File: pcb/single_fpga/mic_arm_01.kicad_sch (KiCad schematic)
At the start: 18 parts, among them U10 IM72D128V01XTMA1, U11 IM72D128V01XTMA1, U12 IM72D128V01XTMA1, U13 IM72D128V01XTMA1, U14 IM72D128V01XTMA1, U15 IM72D128V01XTMA1, U16 IM72D128V01XTMA1, U17 IM72D128V01XTMA1, U18 CDCLVC1108PW

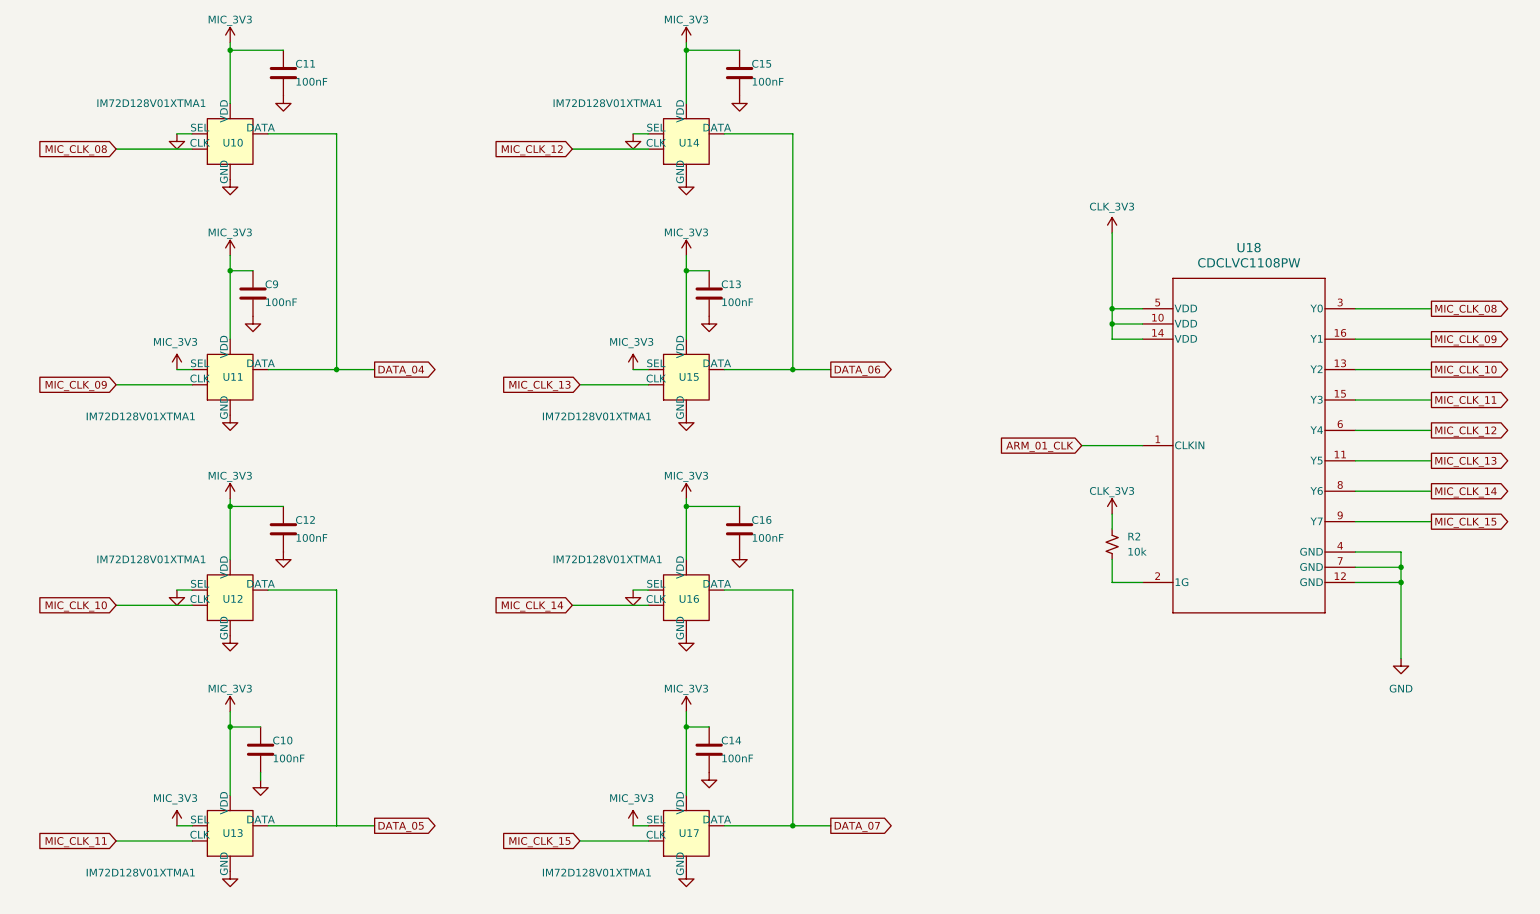
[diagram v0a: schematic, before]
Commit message: Changed mic symbol to improve readability.
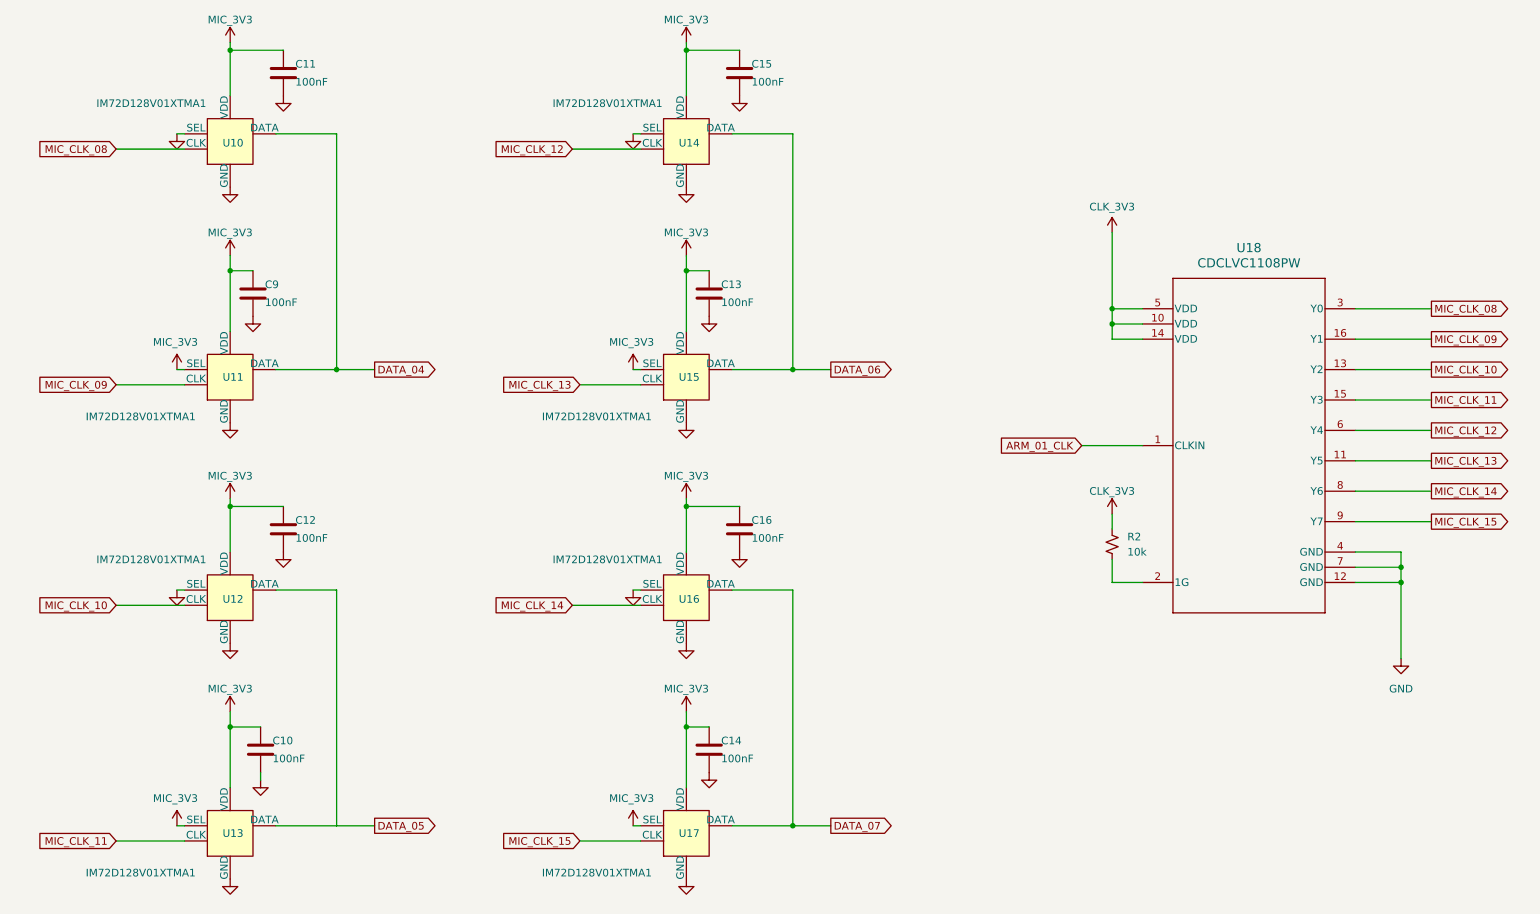
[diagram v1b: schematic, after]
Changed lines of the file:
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@@
 	(wire
 		(pts
-			(xy 127 119.38) (xy 129.54 119.38)
+			(xy 127 119.38) (xy 128.27 119.38)
 		)
 		(stroke
@@
 	(wire
 		(pts
-			(xy 118.11 161.29) (xy 129.54 161.29)
+			(xy 118.11 161.29) (xy 128.27 161.29)
 		)
 		(stroke
@@
 	(wire
 		(pts
-			(xy 59.69 66.04) (xy 59.69 77.47)
+			(xy 59.69 66.04) (xy 59.69 76.2)
 		)
 		(stroke
@@
 	(wire
 		(pts
-			(xy 135.89 105.41) (xy 135.89 114.3)
+			(xy 135.89 105.41) (xy 135.89 113.03)
 		)
 		(stroke
@@
 	(wire
 		(pts
-			(xy 116.84 45.72) (xy 129.54 45.72)
+			(xy 116.84 45.72) (xy 128.27 45.72)
 		)
 		(stroke
@@
 	(wire
 		(pts
-			(xy 40.64 121.92) (xy 53.34 121.92)
+			(xy 40.64 121.92) (xy 52.07 121.92)
 		)
 		(stroke
@@
 	(wire
 		(pts
-			(xy 66.04 158.75) (xy 77.47 158.75)
+			(xy 67.31 158.75) (xy 77.47 158.75)
 		)
 		(stroke
@@
 	(wire
 		(pts
-			(xy 59.69 142.24) (xy 59.69 153.67)
+			(xy 59.69 142.24) (xy 59.69 152.4)
 		)
 		(stroke
@@
 	(wire
 		(pts
-			(xy 153.67 43.18) (xy 142.24 43.18)
+			(xy 153.67 43.18) (xy 143.51 43.18)
 		)
 		(stroke
@@
 	(wire
 		(pts
-			(xy 50.8 82.55) (xy 53.34 82.55)
+			(xy 50.8 82.55) (xy 52.07 82.55)
 		)
 		(stroke
@@
 	(wire
 		(pts
-			(xy 153.67 119.38) (xy 142.24 119.38)
+			(xy 153.67 119.38) (xy 143.51 119.38)
 		)
 		(stroke
@@
 	(wire
 		(pts
-			(xy 40.64 85.09) (xy 53.34 85.09)
+			(xy 40.64 85.09) (xy 52.07 85.09)
 		)
 		(stroke
@@
 	(wire
 		(pts
-			(xy 116.84 121.92) (xy 129.54 121.92)
+			(xy 116.84 121.92) (xy 128.27 121.92)
 		)
 		(stroke
@@
 	(wire
 		(pts
-			(xy 77.47 43.18) (xy 66.04 43.18)
+			(xy 77.47 43.18) (xy 67.31 43.18)
 		)
 		(stroke
@@
 	(wire
 		(pts
-			(xy 127 43.18) (xy 129.54 43.18)
+			(xy 127 43.18) (xy 128.27 43.18)
 		)
 		(stroke
@@
 	(wire
 		(pts
-			(xy 127 158.75) (xy 129.54 158.75)
+			(xy 127 158.75) (xy 128.27 158.75)
 		)
 		(stroke
@@
 	(wire
 		(pts
-			(xy 59.69 105.41) (xy 59.69 114.3)
+			(xy 59.69 105.41) (xy 59.69 113.03)
 		)
 		(stroke
@@
 	(wire
 		(pts
-			(xy 135.89 29.21) (xy 135.89 38.1)
+			(xy 135.89 29.21) (xy 135.89 36.83)
 		)
 		(stroke
@@
 	(wire
 		(pts
-			(xy 118.11 85.09) (xy 129.54 85.09)
+			(xy 118.11 85.09) (xy 128.27 85.09)
 		)
 		(stroke
@@
 	(wire
 		(pts
-			(xy 40.64 45.72) (xy 53.34 45.72)
+			(xy 40.64 45.72) (xy 52.07 45.72)
 		)
 		(stroke
@@
 	(wire
 		(pts
-			(xy 50.8 158.75) (xy 53.34 158.75)
+			(xy 50.8 158.75) (xy 52.07 158.75)
 		)
 		(stroke
@@
 	(wire
 		(pts
-			(xy 50.8 43.18) (xy 53.34 43.18)
+			(xy 50.8 43.18) (xy 52.07 43.18)
 		)
 		(stroke
@@
 	(wire
 		(pts
-			(xy 135.89 66.04) (xy 135.89 77.47)
+			(xy 135.89 66.04) (xy 135.89 76.2)
 		)
 		(stroke
@@
 	(wire
 		(pts
-			(xy 77.47 119.38) (xy 66.04 119.38)
+			(xy 77.47 119.38) (xy 67.31 119.38)
 		)
 		(stroke
@@
 	(wire
 		(pts
-			(xy 142.24 82.55) (xy 153.67 82.55)
+			(xy 143.51 82.55) (xy 153.67 82.55)
 		)
 		(stroke
@@
 	(wire
 		(pts
-			(xy 50.8 119.38) (xy 53.34 119.38)
+			(xy 50.8 119.38) (xy 52.07 119.38)
 		)
 		(stroke
@@
 	(wire
 		(pts
-			(xy 66.04 82.55) (xy 77.47 82.55)
+			(xy 67.31 82.55) (xy 77.47 82.55)
 		)
 		(stroke
@@
 	(wire
 		(pts
-			(xy 142.24 158.75) (xy 153.67 158.75)
+			(xy 143.51 158.75) (xy 153.67 158.75)
 		)
 		(stroke
@@
 	(wire
 		(pts
-			(xy 40.64 161.29) (xy 53.34 161.29)
+			(xy 40.64 161.29) (xy 52.07 161.29)
 		)
 		(stroke
@@
 	(wire
 		(pts
-			(xy 59.69 29.21) (xy 59.69 38.1)
+			(xy 59.69 29.21) (xy 59.69 36.83)
 		)
 		(stroke
@@
 	(wire
 		(pts
-			(xy 127 82.55) (xy 129.54 82.55)
+			(xy 127 82.55) (xy 128.27 82.55)
 		)
 		(stroke
@@
 	(wire
 		(pts
-			(xy 135.89 142.24) (xy 135.89 153.67)
+			(xy 135.89 142.24) (xy 135.89 152.4)
 		)
 		(stroke
@@
 	(symbol
 		(lib_id "power:GND")
-		(at 59.69 50.8 0)
+		(at 59.69 52.07 0)
 		(unit 1)
 		(body_style 1)
@@
 	(symbol
 		(lib_id "power:GND")
-		(at 135.89 50.8 0)
+		(at 135.89 52.07 0)
 		(unit 1)
 		(body_style 1)
@@
 	(symbol
 		(lib_id "power:GND")
-		(at 59.69 166.37 0)
+		(at 59.69 167.64 0)
 		(unit 1)
 		(body_style 1)
@@
 	(symbol
 		(lib_id "power:GND")
-		(at 135.89 127 0)
+		(at 135.89 128.27 0)
 		(unit 1)
 		(body_style 1)
@@
 	(symbol
 		(lib_id "power:GND")
-		(at 135.89 166.37 0)
+		(at 135.89 167.64 0)
 		(unit 1)
 		(body_style 1)
@@
 	(symbol
 		(lib_id "power:GND")
-		(at 59.69 127 0)
+		(at 59.69 128.27 0)
 		(unit 1)
 		(body_style 1)
@@
 	(symbol
 		(lib_id "power:GND")
-		(at 59.69 90.17 0)
+		(at 59.69 91.44 0)
 		(unit 1)
 		(body_style 1)
@@
 	(symbol
 		(lib_id "power:GND")
-		(at 135.89 90.17 0)
+		(at 135.89 91.44 0)
 		(unit 1)
 		(body_style 1)

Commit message: Used new mic symbol and cleaned up.
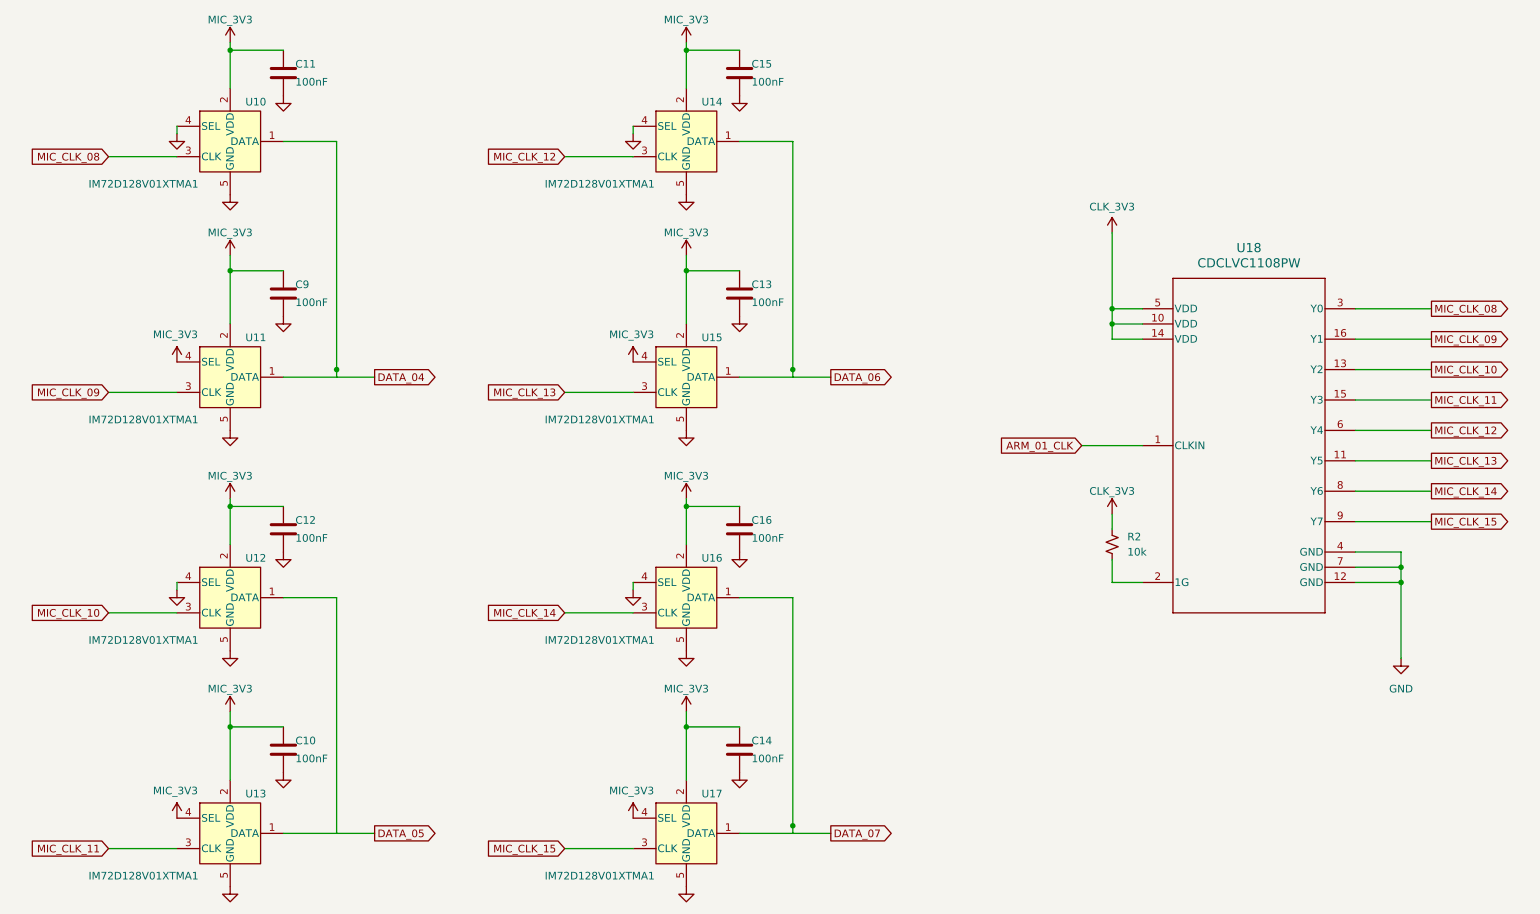
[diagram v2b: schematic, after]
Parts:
- U10, U11, U12, U13, U14, U15, U16, U17: footprint IM72D128:IFX-PG-LLGA-5-4 -> (none)
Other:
- moved on the sheet: C10, C13, C14, C9

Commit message: Fixed all DRC warnings.
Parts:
- U10, U11, U12, U13, U14, U15, U16, U17: footprint (none) -> IM72D128:IFX-PG-LLGA-5-4
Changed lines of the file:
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@@
 			)
 		)
-		(property "Footprint" ""
+		(property "Footprint" "IM72D128:IFX-PG-LLGA-5-4"
 			(at 59.69 44.45 0)
 			(hide yes)
@@
 			)
 		)
-		(property "Footprint" ""
+		(property "Footprint" "IM72D128:IFX-PG-LLGA-5-4"
 			(at 59.69 83.82 0)
 			(hide yes)
@@
 			)
 		)
-		(property "Footprint" ""
+		(property "Footprint" "IM72D128:IFX-PG-LLGA-5-4"
 			(at 135.89 83.82 0)
 			(hide yes)
@@
 			)
 		)
-		(property "Footprint" ""
+		(property "Footprint" "IM72D128:IFX-PG-LLGA-5-4"
 			(at 59.69 120.65 0)
 			(hide yes)
@@
 			)
 		)
-		(property "Footprint" ""
+		(property "Footprint" "IM72D128:IFX-PG-LLGA-5-4"
 			(at 135.89 44.45 0)
 			(hide yes)
@@
 			)
 		)
-		(property "Footprint" ""
+		(property "Footprint" "IM72D128:IFX-PG-LLGA-5-4"
 			(at 135.89 120.65 0)
 			(hide yes)
@@
 			)
 		)
-		(property "Footprint" ""
+		(property "Footprint" "IM72D128:IFX-PG-LLGA-5-4"
 			(at 59.69 160.02 0)
 			(hide yes)
@@
 			)
 		)
-		(property "Footprint" ""
+		(property "Footprint" "IM72D128:IFX-PG-LLGA-5-4"
 			(at 135.89 160.02 0)
 			(hide yes)

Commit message: Aligned mic and cap ref des numbers.
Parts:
- renumbered C9 to C10, C12 to C11, C10 to C12, C15 to C13, C13 to C14, C16 to C15, C14 to C16, C11 to C9, U11 to U10, U12 to U11, U13 to U12, U14 to U13, U15 to U14, U16 to U15, U17 to U16, U10 to U9, U18 to U98
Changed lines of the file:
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@@
 		(dnp no)
 		(fields_autoplaced yes)
-		(property "Reference" "U18"
+		(property "Reference" "U98"
 			(at 229.87 62.23 0)
 			(show_name no)
@@
 			(project "mic_array"
 				(path "/12638caa-1907-413e-8e98-06abbbf6ccbc/2e46394f-4741-4d6d-9c50-8b81cff9872d"
-					(reference "U18")
+					(reference "U98")
 					(unit 1)
 				)
@@
 		(in_pos_files yes)
 		(dnp no)
-		(property "Reference" "C13"
+		(property "Reference" "C14"
 			(at 146.78 68.35 0)
 			(show_name no)
@@
 			(project "mic_array"
 				(path "/12638caa-1907-413e-8e98-06abbbf6ccbc/2e46394f-4741-4d6d-9c50-8b81cff9872d"
-					(reference "C13")
+					(reference "C14")
 					(unit 1)
 				)
@@
 		(in_pos_files yes)
 		(dnp no)
-		(property "Reference" "C12"
+		(property "Reference" "C11"
 			(at 70.58 107.72 0)
 			(show_name no)
@@
 			(project "mic_array"
 				(path "/12638caa-1907-413e-8e98-06abbbf6ccbc/2e46394f-4741-4d6d-9c50-8b81cff9872d"
-					(reference "C12")
+					(reference "C11")
 					(unit 1)
 				)
@@
 		(in_pos_files yes)
 		(dnp no)
-		(property "Reference" "U10"
+		(property "Reference" "U9"
 			(at 62.23 37.846 0)
 			(show_name no)
@@
 			(project "mic_array"
 				(path "/12638caa-1907-413e-8e98-06abbbf6ccbc/2e46394f-4741-4d6d-9c50-8b81cff9872d"
-					(reference "U10")
+					(reference "U9")
 					(unit 1)
 				)
@@
 		(in_pos_files yes)
 		(dnp no)
-		(property "Reference" "U11"
+		(property "Reference" "U10"
 			(at 62.23 77.216 0)
 			(show_name no)
@@
 			(project "mic_array"
 				(path "/12638caa-1907-413e-8e98-06abbbf6ccbc/2e46394f-4741-4d6d-9c50-8b81cff9872d"
-					(reference "U11")
+					(reference "U10")
 					(unit 1)
 				)
@@
 		(in_pos_files yes)
 		(dnp no)
-		(property "Reference" "U15"
+		(property "Reference" "U14"
 			(at 138.43 77.216 0)
 			(show_name no)
@@
 			(project "mic_array"
 				(path "/12638caa-1907-413e-8e98-06abbbf6ccbc/2e46394f-4741-4d6d-9c50-8b81cff9872d"
-					(reference "U15")
+					(reference "U14")
 					(unit 1)
 				)
@@
 		(in_pos_files yes)
 		(dnp no)
-		(property "Reference" "U12"
+		(property "Reference" "U11"
 			(at 62.23 114.046 0)
 			(show_name no)
@@
 			(project "mic_array"
 				(path "/12638caa-1907-413e-8e98-06abbbf6ccbc/2e46394f-4741-4d6d-9c50-8b81cff9872d"
-					(reference "U12")
+					(reference "U11")
 					(unit 1)
 				)
@@
 		(in_pos_files yes)
 		(dnp no)
-		(property "Reference" "U14"
+		(property "Reference" "U13"
 			(at 138.43 37.846 0)
 			(show_name no)
@@
 			(project "mic_array"
 				(path "/12638caa-1907-413e-8e98-06abbbf6ccbc/2e46394f-4741-4d6d-9c50-8b81cff9872d"
-					(reference "U14")
+					(reference "U13")
 					(unit 1)
 				)
@@
 		(in_pos_files yes)
 		(dnp no)
-		(property "Reference" "C14"
+		(property "Reference" "C16"
 			(at 146.78 144.55 0)
 			(show_name no)
@@
 			(project "mic_array"
 				(path "/12638caa-1907-413e-8e98-06abbbf6ccbc/2e46394f-4741-4d6d-9c50-8b81cff9872d"
-					(reference "C14")
+					(reference "C16")
 					(unit 1)
 				)
@@
 		(in_pos_files yes)
 		(dnp no)
-		(property "Reference" "C11"
+		(property "Reference" "C9"
 			(at 70.58 31.52 0)
 			(show_name no)
@@
 			(project "mic_array"
 				(path "/12638caa-1907-413e-8e98-06abbbf6ccbc/2e46394f-4741-4d6d-9c50-8b81cff9872d"
-					(reference "C11")
+					(reference "C9")
 					(unit 1)
 				)
@@
 		(in_pos_files yes)
 		(dnp no)
-		(property "Reference" "C15"
+		(property "Reference" "C13"
 			(at 146.78 31.52 0)
 			(show_name no)
@@
 			(project "mic_array"
 				(path "/12638caa-1907-413e-8e98-06abbbf6ccbc/2e46394f-4741-4d6d-9c50-8b81cff9872d"
-					(reference "C15")
+					(reference "C13")
 					(unit 1)
 				)
@@
 		(in_pos_files yes)
 		(dnp no)
-		(property "Reference" "C10"
+		(property "Reference" "C12"
 			(at 70.58 144.55 0)
 			(show_name no)
@@
 			(project "mic_array"
 				(path "/12638caa-1907-413e-8e98-06abbbf6ccbc/2e46394f-4741-4d6d-9c50-8b81cff9872d"
-					(reference "C10")
+					(reference "C12")
 					(unit 1)
 				)
@@
 		(in_pos_files yes)
 		(dnp no)
-		(property "Reference" "U16"
+		(property "Reference" "U15"
 			(at 138.43 114.046 0)
 			(show_name no)
@@
 			(project "mic_array"
 				(path "/12638caa-1907-413e-8e98-06abbbf6ccbc/2e46394f-4741-4d6d-9c50-8b81cff9872d"
-					(reference "U16")
+					(reference "U15")
 					(unit 1)
 				)
@@
 		(in_pos_files yes)
 		(dnp no)
-		(property "Reference" "U13"
+		(property "Reference" "U12"
 			(at 62.23 153.416 0)
 			(show_name no)
@@
 			(project "mic_array"
 				(path "/12638caa-1907-413e-8e98-06abbbf6ccbc/2e46394f-4741-4d6d-9c50-8b81cff9872d"
-					(reference "U13")
+					(reference "U12")
 					(unit 1)
 				)
@@
 		(in_pos_files yes)
 		(dnp no)
-		(property "Reference" "U17"
+		(property "Reference" "U16"
 			(at 138.43 153.416 0)
 			(show_name no)
@@
 			(project "mic_array"
 				(path "/12638caa-1907-413e-8e98-06abbbf6ccbc/2e46394f-4741-4d6d-9c50-8b81cff9872d"
-					(reference "U17")
+					(reference "U16")
 					(unit 1)
 				)
@@
 		(in_pos_files yes)
 		(dnp no)
-		(property "Reference" "C9"
+		(property "Reference" "C10"
 			(at 70.58 68.35 0)
 			(show_name no)
@@
 			(project "mic_array"
 				(path "/12638caa-1907-413e-8e98-06abbbf6ccbc/2e46394f-4741-4d6d-9c50-8b81cff9872d"
-					(reference "C9")
+					(reference "C10")
 					(unit 1)
 				)
@@
 		(in_pos_files yes)
 		(dnp no)
-		(property "Reference" "C16"
+		(property "Reference" "C15"
 			(at 146.78 107.72 0)
 			(show_name no)
@@
 			(project "mic_array"
 				(path "/12638caa-1907-413e-8e98-06abbbf6ccbc/2e46394f-4741-4d6d-9c50-8b81cff9872d"
-					(reference "C16")
+					(reference "C15")
 					(unit 1)
 				)

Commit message: Added decoupling caps. ERC-/DRC-clean.
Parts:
- added C115: 100nF, Capacitor_SMD:C_0603_1608Metric, symbol Device:C
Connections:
- net CLK_3V3: now also C115.1
- net GND: now also C115.2
